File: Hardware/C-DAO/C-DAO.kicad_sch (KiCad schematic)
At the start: 63 parts, among them J1 DIN-5, J2 Bus-connector, J3 AudioJack2, J5 Conn_02x03_Odd_Even, SW1 SW_Push_Dual, SW2 SW_Push_Dual, SW3 SW_Push_Dual, SW4 SW_Push_Dual, U1 ATmega328P-A, U2 L7805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

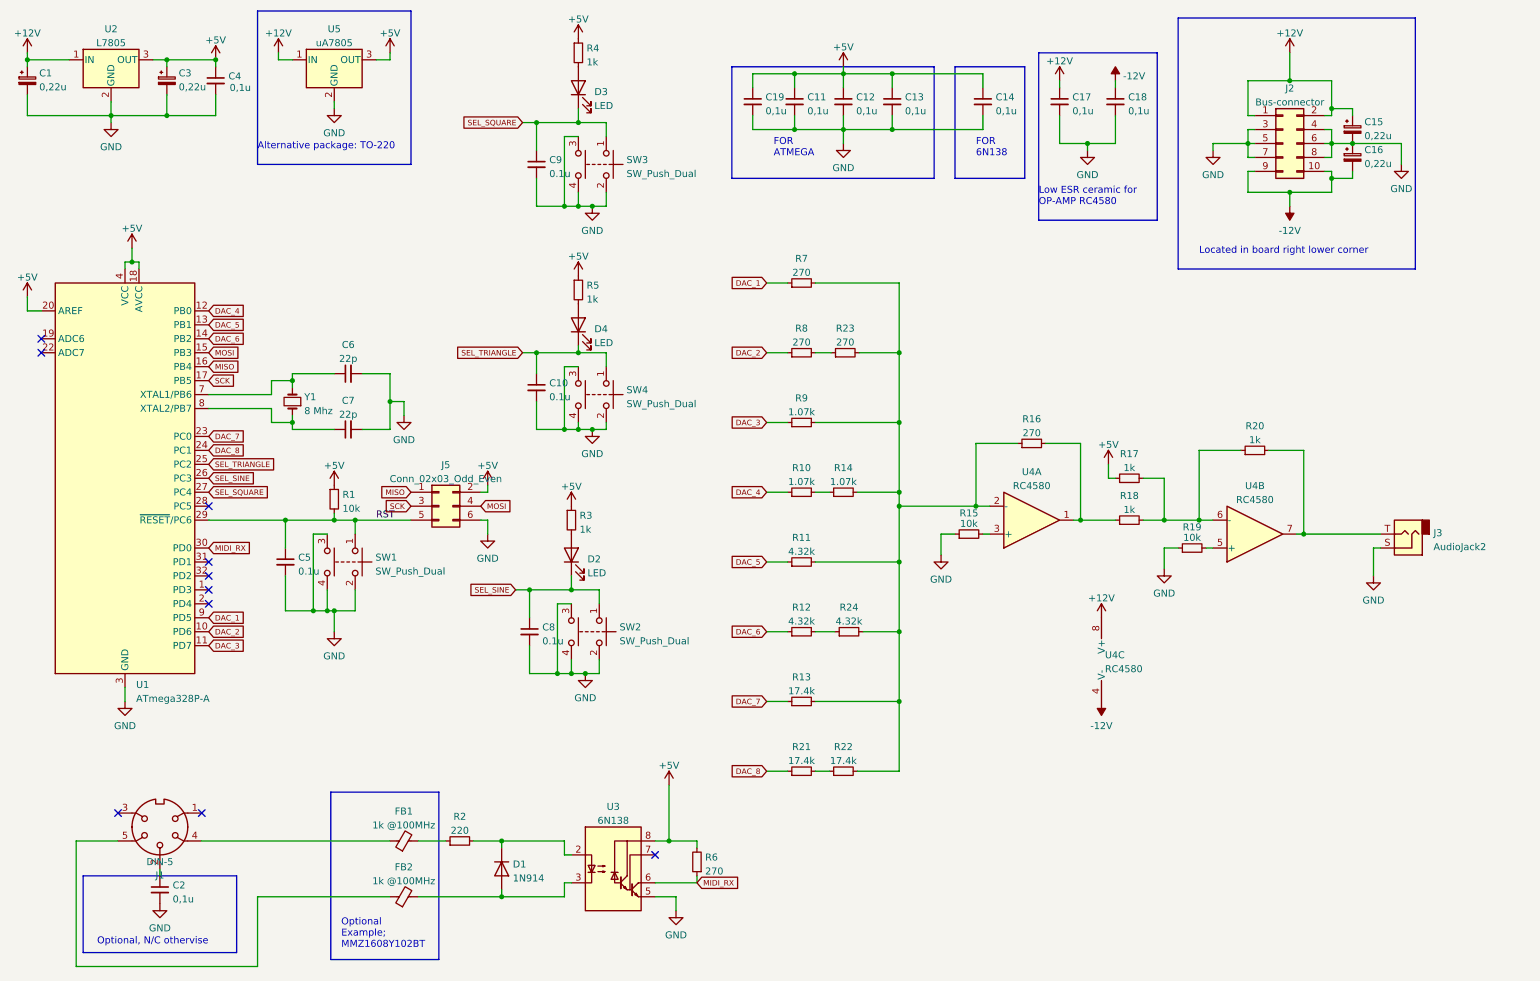
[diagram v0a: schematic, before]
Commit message: Add production files and latest pcb files with bom
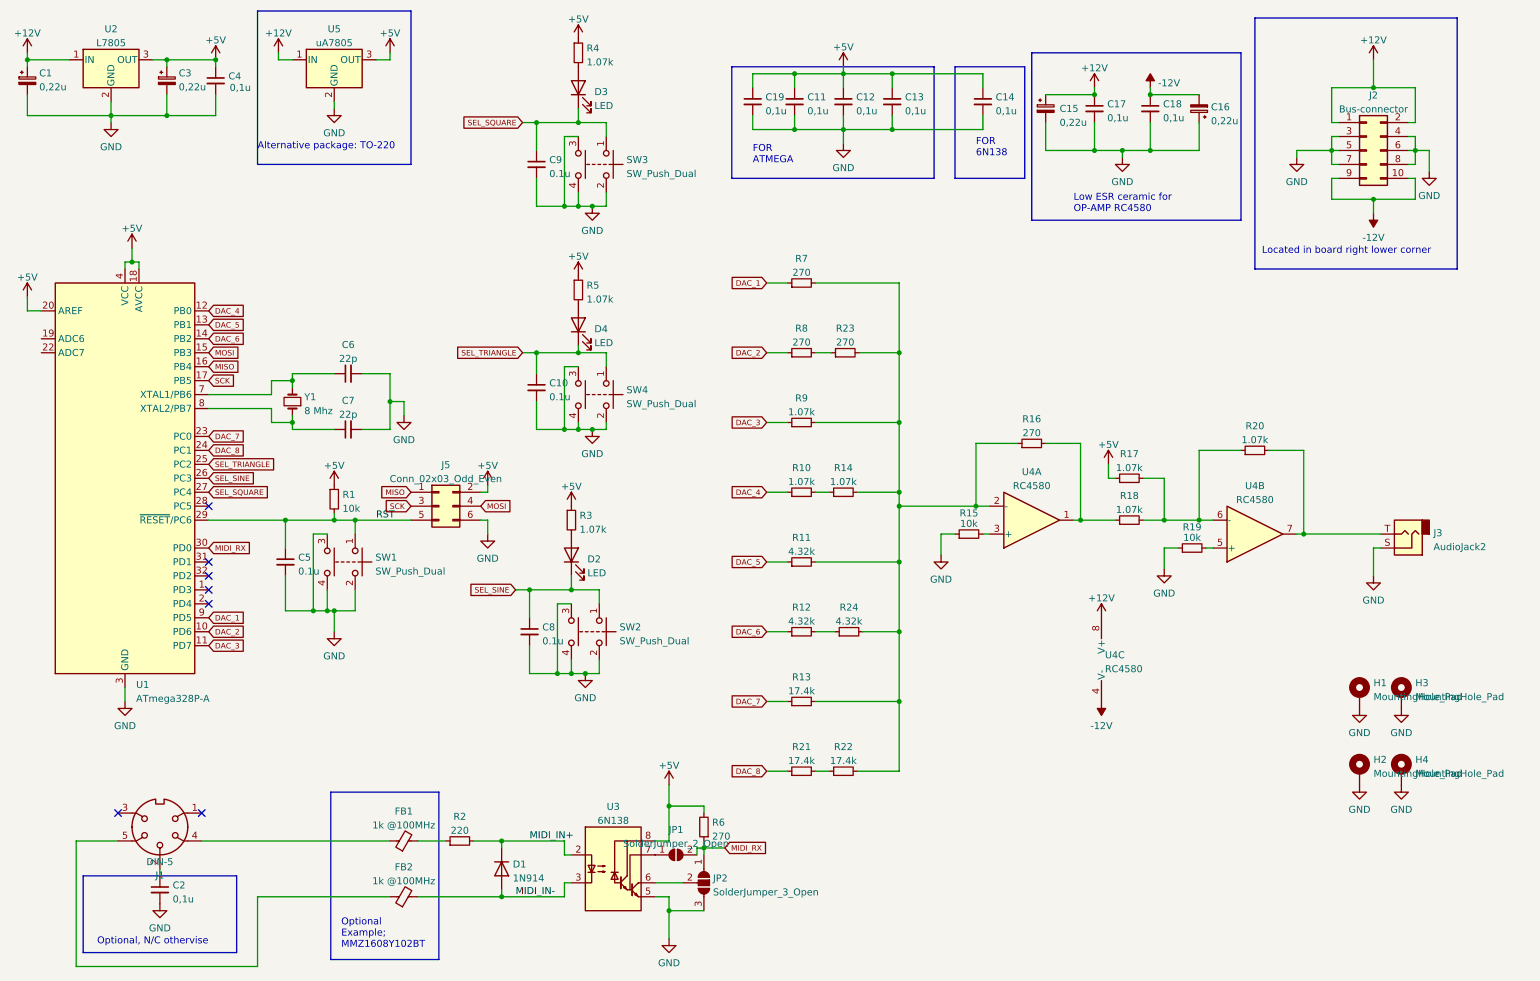
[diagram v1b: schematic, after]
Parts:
- added H1, H2, H3, H4: MountingHole_Pad, MountingHole:MountingHole_3.2mm_M3_DIN965_Pad_TopBottom, symbol Mechanical:MountingHole_Pad
- added JP1: SolderJumper_2_Open, Jumper:SolderJumper-2_P1.3mm_Open_Pad1.0x1.5mm, symbol Jumper:SolderJumper_2_Open
- added JP2: SolderJumper_3_Open, Jumper:SolderJumper-3_P1.3mm_Open_Pad1.0x1.5mm_NumberLabels, symbol Jumper:SolderJumper_3_Open
- D2, D3, D4: footprint LED_THT:LED_D5.0mm_Horizontal_O6.35mm_Z9.0mm -> LED_THT:LED_D5.0mm_Horizontal_O6.35mm_Z15.0mm
- J1: footprint CustomConnectors:5-pin DIN socket vertical -> footprints:5-pin DIN socket vertical
- R17, R18, R20, R3, R4, R5: value 1k -> 1.07k
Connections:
- net GND: now also H1.1, H2.1, H3.1, H4.1, JP2.3 (B)
- net MIDI_RX: now also JP1.2 (B), JP2.1 (A); no longer U3.6 (VO2)
- net MIDI_IN-: now reaches D1.2 (A), FB2.2, U3.3 (C2)
- net MIDI_IN+: now reaches D1.1 (K), R2.2, U3.2 (C1)
- net at U3.7 (VO1): now also JP1.1 (A)
- new net: JP2.2 (C), U3.6 (VO2)
- no-connect marks 10 -> 7
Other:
- moved on the sheet: C15, C16, C17, C18, J2, R6

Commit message: Update 3d models and create wrl-model from board
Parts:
- J3: footprint CustomConnectors:Cliff CL13843G 3.5mm mono jack -> footprints:Cliff CL13843G 3.5mm mono jack
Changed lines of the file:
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@@
       (effects (font (size 1.27 1.27)) (justify right))
     )
-    (property "Footprint" "CustomConnectors:Cliff CL13843G 3.5mm mono jack" (id 2) (at 273.05 109.22 0)
+    (property "Footprint" "footprints:Cliff CL13843G 3.5mm mono jack" (id 2) (at 273.05 109.22 0)
       (effects (font (size 1.27 1.27)) hide)
     )
@@
     )
     (path "/2c3333c1-1d3b-4fef-86cb-fa21eaf94d16"
-      (reference "J3") (unit 1) (value "AudioJack2") (footprint "CustomConnectors:Cliff CL13843G 3.5mm mono jack")
+      (reference "J3") (unit 1) (value "AudioJack2") (footprint "footprints:Cliff CL13843G 3.5mm mono jack")
     )
     (path "/0f4e15c9-19dc-4733-be5f-cbe0672a543b"
